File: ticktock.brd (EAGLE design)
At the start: 61 x 67.3 mm, 64 parts, among them IC1 ATMEGA644A, IC2 AD8611RM, IC3 REF200U, J1 AVR_SPI_PRG_6NS, Q1 MOSFET-NCHANNEL2N7002PW, Q2 MOSFET-NCHANNELBSS138, Q3 MOSFET-NCHANNELBSS138, U1 MAX232SOIC16, U2 OSCILLATORSMD, U3 FT232RLSSOP, U4 BMP180

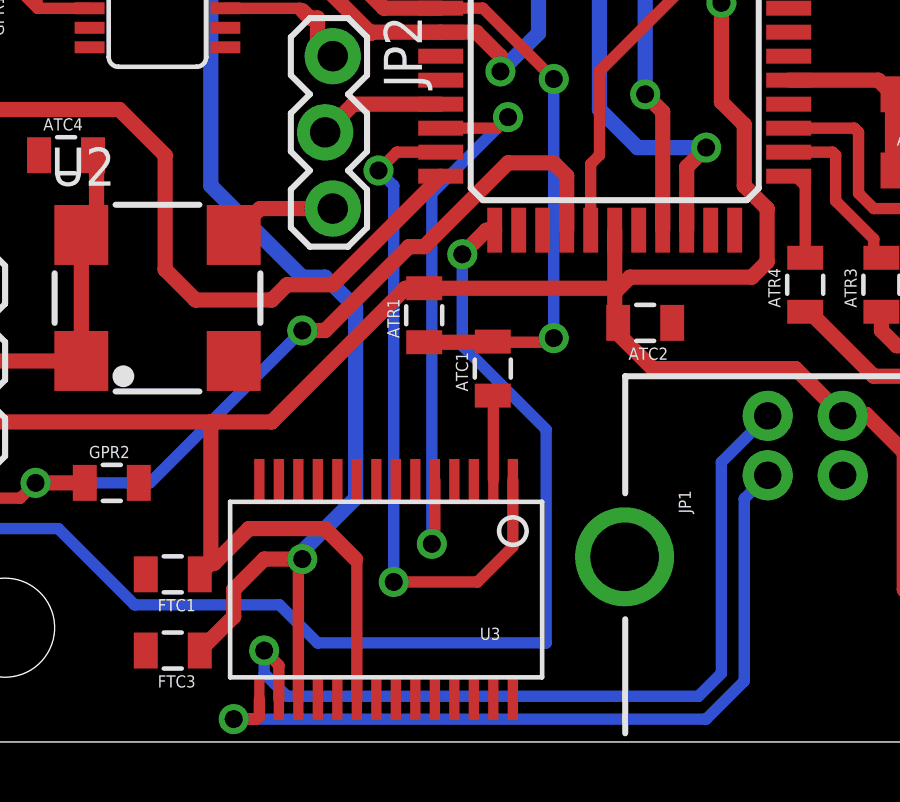
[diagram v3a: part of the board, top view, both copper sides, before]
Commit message: Add power to pin 4 of FTDI chip.
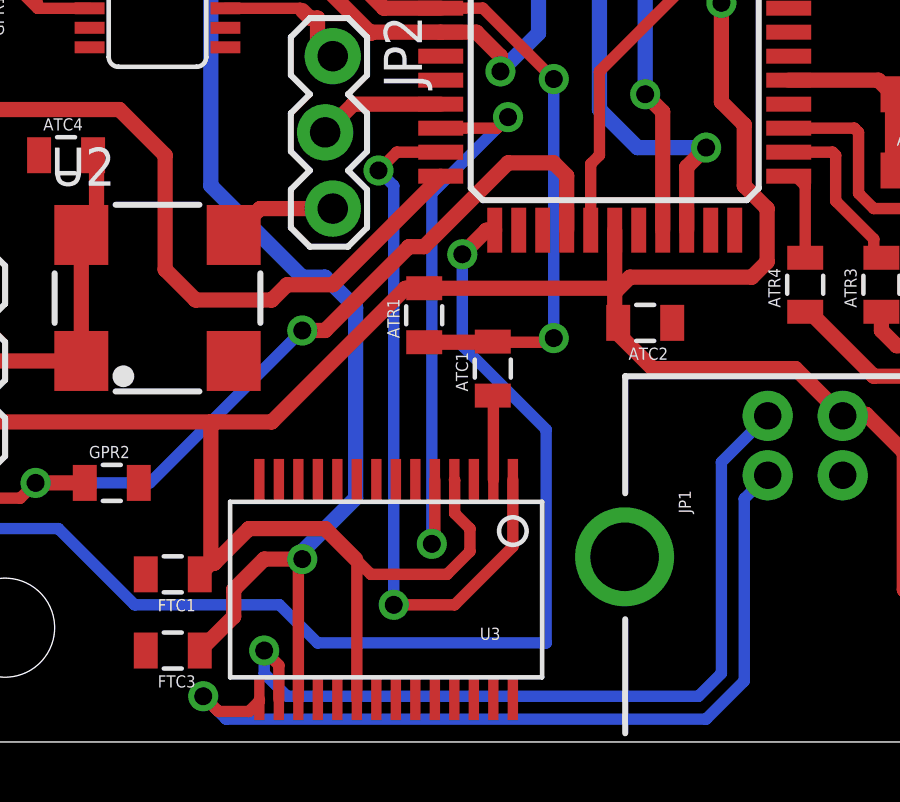
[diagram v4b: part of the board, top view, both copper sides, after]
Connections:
- removed net VCCIO: U3.4
- net 5V: now also U3.4
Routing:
- net 5V: track 295.6 -> 302.5 mm
- net N$12: track 26.2 -> 28.3 mm
- net USB_TX: track 22.9 -> 24.0 mm
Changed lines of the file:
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@@
 </class>
 </classes>
-<designrules name="default">
+<designrules name="default *">
 <description language="de">&lt;b&gt;EAGLE Design Rules&lt;/b&gt;
 &lt;p&gt;
@@
 <param name="mdViaViaSameLayer" value="8mil"/>
 <param name="mnLayersViaInSmd" value="2"/>
-<param name="mdCopperDimension" value="40mil"/>
+<param name="mdCopperDimension" value="20mil"/>
 <param name="mdDrill" value="8mil"/>
 <param name="mdSmdStop" value="0mil"/>
 <param name="msWidth" value="10mil"/>
-<param name="msDrill" value="24mil"/>
+<param name="msDrill" value="23mil"/>
 <param name="msMicroVia" value="9.99mm"/>
 <param name="msBlindViaRatio" value="0.5"/>
@@
 <wire x1="20.597" y1="25.106" x2="21.804" y2="25.106" width="0.381" layer="1"/>
 <wire x1="21.804" y1="25.106" x2="21.844" y2="25.146" width="0.381" layer="1"/>
+<contactref element="U3" pad="4"/>
+<wire x1="29.505" y1="6.055" x2="29.972" y2="5.588" width="0.381" layer="1"/>
+<wire x1="29.972" y1="5.588" x2="32.512" y2="5.588" width="0.381" layer="1"/>
+<wire x1="32.512" y1="5.588" x2="33.274" y2="6.35" width="0.381" layer="1"/>
+<wire x1="33.274" y1="6.35" x2="33.274" y2="7.112" width="0.381" layer="1"/>
+<wire x1="33.274" y1="7.112" x2="32.766" y2="7.62" width="0.381" layer="1"/>
+<wire x1="32.766" y1="7.62" x2="32.766" y2="8.725" width="0.381" layer="1"/>
+<wire x1="32.766" y1="8.725" x2="32.755" y2="8.736" width="0.381" layer="1"/>
 </signal>
 <signal name="N$1">
@@
 <wire x1="18.862" y1="24.456" x2="18.288" y2="25.03" width="0.381" layer="1"/>
 </signal>
-<signal name="VCCIO">
-<contactref element="U3" pad="4"/>
-</signal>
 <signal name="N$11">
 <contactref element="JP1" pad="D-"/>
@@
 <contactref element="U3" pad="15"/>
 <contactref element="JP1" pad="D+"/>
-<wire x1="26.255" y1="1.424" x2="26.255" y2="0.855" width="0.381" layer="1"/>
-<wire x1="26.255" y1="0.855" x2="26.162" y2="0.762" width="0.381" layer="1"/>
-<wire x1="26.162" y1="0.762" x2="25.4" y2="0.762" width="0.381" layer="1"/>
-<via x="25.4" y="0.762" extent="1-16" drill="0.6"/>
-<wire x1="25.4" y1="0.762" x2="41.148" y2="0.762" width="0.381" layer="16"/>
+<wire x1="26.255" y1="1.424" x2="26.255" y2="1.363" width="0.381" layer="1"/>
+<wire x1="26.255" y1="1.363" x2="25.908" y2="1.016" width="0.381" layer="1"/>
+<wire x1="25.908" y1="1.016" x2="24.892" y2="1.016" width="0.381" layer="1"/>
+<wire x1="24.892" y1="1.016" x2="24.384" y2="1.524" width="0.381" layer="1"/>
+<via x="24.384" y="1.524" extent="1-16" drill="0.6"/>
+<wire x1="24.384" y1="1.524" x2="25.146" y2="0.762" width="0.381" layer="16"/>
+<wire x1="25.146" y1="0.762" x2="41.148" y2="0.762" width="0.381" layer="16"/>
 <wire x1="41.148" y1="0.762" x2="42.418" y2="2.032" width="0.381" layer="16"/>
 <wire x1="42.418" y1="2.032" x2="42.418" y2="8.108" width="0.381" layer="16"/>
@@
 <contactref element="IC1" pad="10"/>
 <wire x1="34.705" y1="8.736" x2="34.705" y2="6.511" width="0.381" layer="1"/>
-<wire x1="34.705" y1="6.511" x2="33.528" y2="5.334" width="0.381" layer="1"/>
-<wire x1="33.528" y1="5.334" x2="30.734" y2="5.334" width="0.381" layer="1"/>
-<via x="30.734" y="5.334" extent="1-16" drill="0.6"/>
-<wire x1="30.734" y1="5.334" x2="30.734" y2="18.542" width="0.381" layer="16"/>
+<wire x1="34.705" y1="6.511" x2="32.766" y2="4.572" width="0.381" layer="1"/>
+<via x="30.734" y="4.572" extent="1-16" drill="0.6"/>
+<wire x1="30.734" y1="4.572" x2="30.734" y2="18.542" width="0.381" layer="16"/>
 <wire x1="30.734" y1="18.542" x2="30.226" y2="19.05" width="0.381" layer="16"/>
 <via x="30.226" y="19.05" extent="1-16" drill="0.6"/>
 <wire x1="30.226" y1="19.05" x2="30.836" y2="19.66" width="0.381" layer="1"/>
 <wire x1="30.836" y1="19.66" x2="32.3" y2="19.66" width="0.381" layer="1"/>
+<wire x1="32.766" y1="4.572" x2="30.734" y2="4.572" width="0.381" layer="1"/>
 </signal>
 <signal name="USB_RX">

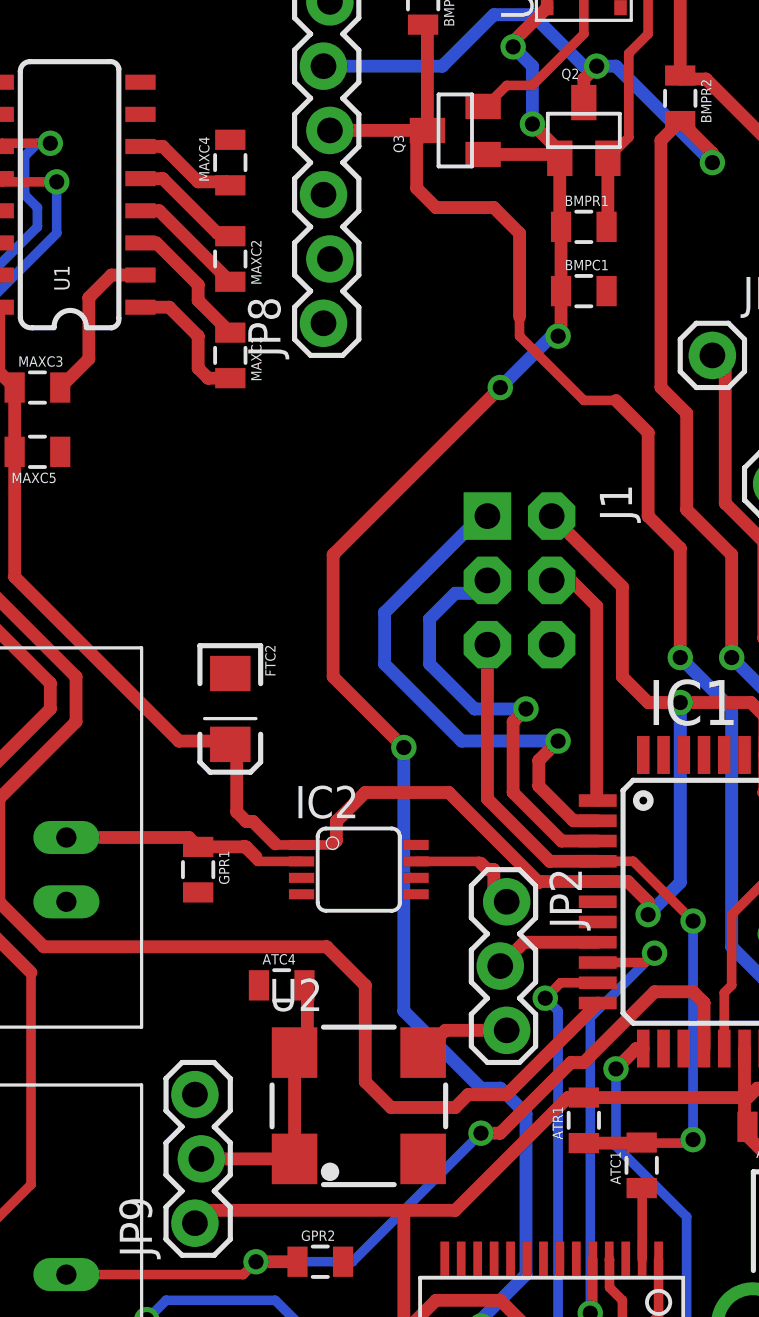
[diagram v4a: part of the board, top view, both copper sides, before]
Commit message: Fix ERC and DRC complaints.  Connect accidentally unconnected nets.
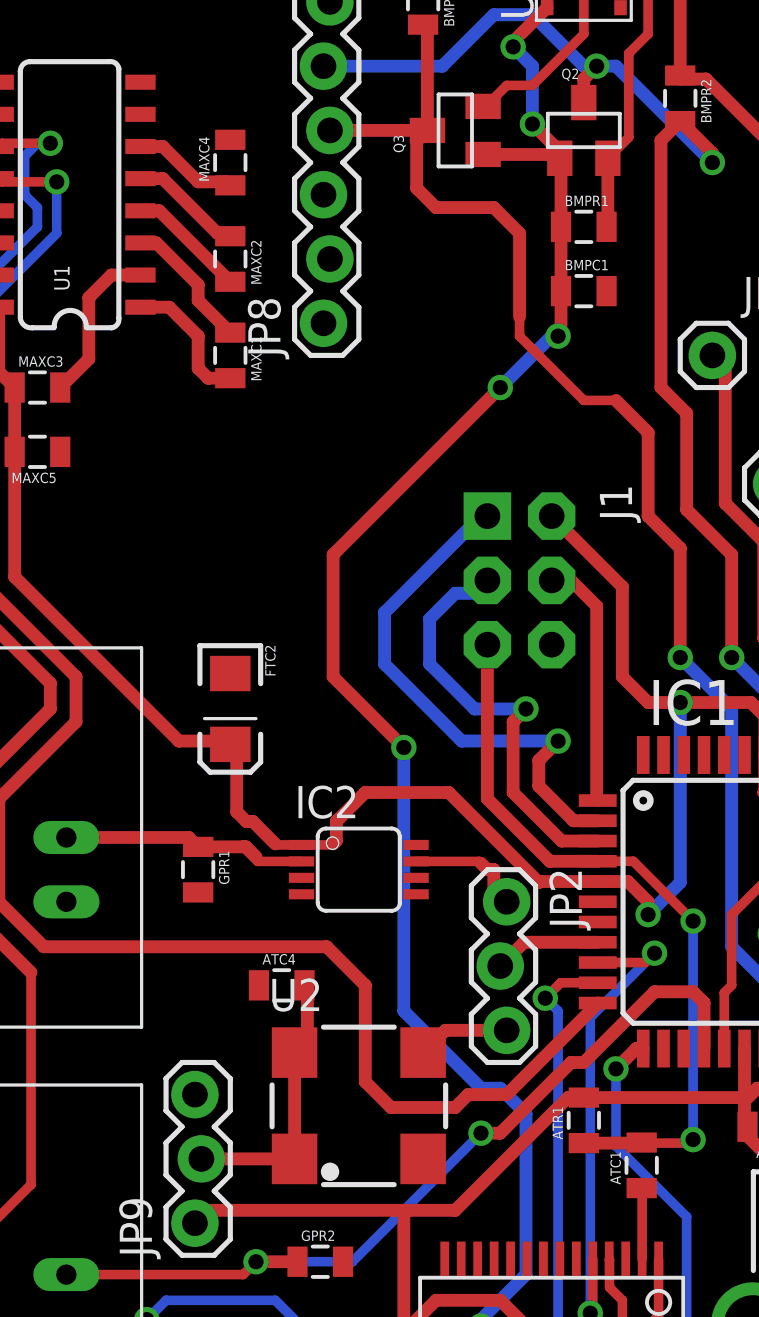
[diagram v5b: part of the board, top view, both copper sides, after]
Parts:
- JP2: value (none) -> 3 Pin
- JP8: value (none) -> 7-Pin
- JP9: value (none) -> 3-Pin
- U$1: value (none) -> OPA381
- X1: value (none) -> RS232
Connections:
- net GND: now also U$1.3, U$1.4
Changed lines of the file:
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@@
 <layer number="35" name="tGlue" color="7" fill="4" visible="no" active="yes"/>
 <layer number="36" name="bGlue" color="7" fill="5" visible="no" active="yes"/>
-<layer number="37" name="tTest" color="7" fill="1" visible="no" active="yes"/>
-<layer number="38" name="bTest" color="7" fill="1" visible="no" active="yes"/>
-<layer number="39" name="tKeepout" color="4" fill="11" visible="yes" active="yes"/>
-<layer number="40" name="bKeepout" color="1" fill="11" visible="yes" active="yes"/>
-<layer number="41" name="tRestrict" color="4" fill="10" visible="yes" active="yes"/>
-<layer number="42" name="bRestrict" color="1" fill="10" visible="yes" active="yes"/>
-<layer number="43" name="vRestrict" color="2" fill="10" visible="yes" active="yes"/>
-<layer number="44" name="Drills" color="7" fill="1" visible="no" active="yes"/>
-<layer number="45" name="Holes" color="7" fill="1" visible="no" active="yes"/>
-<layer number="46" name="Milling" color="3" fill="1" visible="no" active="yes"/>
-<layer number="47" name="Measures" color="7" fill="1" visible="no" active="yes"/>
+<layer number="37" name="tTest" color="7" fill="1" visible="yes" active="yes"/>
+<layer number="38" name="bTest" color="7" fill="1" visible="yes" active="yes"/>
+<layer number="39" name="tKeepout" color="4" fill="11" visible="no" active="yes"/>
+<layer number="40" name="bKeepout" color="1" fill="11" visible="no" active="yes"/>
+<layer number="41" name="tRestrict" color="4" fill="10" visible="no" active="yes"/>
+<layer number="42" name="bRestrict" color="1" fill="10" visible="no" active="yes"/>
+<layer number="43" name="vRestrict" color="2" fill="10" visible="no" active="yes"/>
+<layer number="44" name="Drills" color="7" fill="1" visible="yes" active="yes"/>
+<layer number="45" name="Holes" color="7" fill="1" visible="yes" active="yes"/>
+<layer number="46" name="Milling" color="3" fill="1" visible="yes" active="yes"/>
+<layer number="47" name="Measures" color="7" fill="1" visible="yes" active="yes"/>
 <layer number="48" name="Document" color="7" fill="1" visible="yes" active="yes"/>
 <layer number="49" name="Reference" color="7" fill="1" visible="yes" active="yes"/>
@@
 <element name="MAXC5" library="SparkFun-Capacitors" package="0805" value="1uF" x="10.16" y="40.64" rot="R180"/>
 <element name="MAXC4" library="SparkFun-Capacitors" package="0805" value="1uF" x="17.78" y="52.07" rot="R90"/>
-<element name="X1" library="SparkFun-Connectors" package="DB9" value="" x="3.81" y="50.8" rot="R90"/>
+<element name="X1" library="SparkFun-Connectors" package="DB9" value="RS232" x="3.81" y="50.8" rot="R90"/>
 <element name="GPS_10MHZ_IN" library="SparkFun-Connectors" package="BNC" value="BNCPTH" x="11.303" y="25.4" rot="R90"/>
 <element name="GPS_1PPS_IN" library="SparkFun-Connectors" package="BNC" value="BNCPTH" x="11.303" y="8.128" rot="R90"/>
@@
 <element name="U2" library="SparkFun-FreqCtrl" package="CRYSTAL-SMD-7X5" value="OSCILLATORSMD" x="20.32" y="12.7"/>
 <element name="ATC4" library="SparkFun-Capacitors" package="0805" value="0.01uF" x="19.812" y="19.558"/>
-<element name="JP2" library="SparkFun-Connectors" package="1X03_LOCK" value="" x="28.575" y="22.86" rot="R270"/>
+<element name="JP2" library="SparkFun-Connectors" package="1X03_LOCK" value="3 Pin" x="28.575" y="22.86" rot="R270"/>
 <element name="IC2" library="analog-devices" package="MSOP08" value="AD8611RM" x="22.86" y="24.13" rot="R270">
 <attribute name="OC_NEWARK" value="19M8930" x="22.86" y="24.13" size="1.778" layer="27" rot="R270" display="off"/>
@@
 <element name="CFB" library="SparkFun-Capacitors" package="0805" value="??" x="50.8" y="24.13" rot="R90"/>
 <element name="AMPC1" library="SparkFun-Capacitors" package="0805" value="1uF" x="59.69" y="24.13" rot="R90"/>
-<element name="U$1" library="tickTockLibrary" package="MSOP08" value="" x="56.134" y="20.32" rot="R270"/>
+<element name="U$1" library="tickTockLibrary" package="MSOP08" value="OPA381" x="56.134" y="20.32" rot="R270"/>
 <element name="U4" library="SparkFun-Sensors" package="BMP180" value="BMP180" x="31.75" y="59.69" rot="R90"/>
 <element name="IC3" library="burr-brown" package="SO08" value="REF200U" x="49.53" y="35.56" rot="R270"/>
@@
 <element name="JP6" library="SparkFun-Connectors" package="1X01" value="M01PTH" x="45.72" y="41.91"/>
 <element name="JP7" library="SparkFun-Connectors" package="1X01" value="M01PTH" x="57.15" y="26.67"/>
-<element name="JP8" library="SparkFun-Connectors" package="1X07_LOCK" value="" x="21.59" y="45.72" rot="R90"/>
+<element name="JP8" library="SparkFun-Connectors" package="1X07_LOCK" value="7-Pin" x="21.59" y="45.72" rot="R90"/>
 <element name="STANDOFF1" library="SparkFun-Electromechanical" package="STAND-OFF" value="STAND-OFF" x="57.15" y="63.5"/>
 <element name="STANDOFF2" library="SparkFun-Electromechanical" package="STAND-OFF" value="STAND-OFF" x="10.16" y="63.5"/>
 <element name="STANDOFF3" library="SparkFun-Electromechanical" package="STAND-OFF" value="STAND-OFF" x="56.642" y="15.24"/>
 <element name="STANDOFF4" library="SparkFun-Electromechanical" package="STAND-OFF" value="STAND-OFF" x="17.78" y="3.81"/>
-<element name="JP9" library="SparkFun-Connectors" package="1X03_LOCK" value="" x="16.51" y="10.16" rot="R90"/>
+<element name="JP9" library="SparkFun-Connectors" package="1X03_LOCK" value="3-Pin" x="16.51" y="10.16" rot="R90"/>
 </elements>
 <signals>
@@
 <contactref element="JP8" pad="1"/>
 <contactref element="PKG-CABLE" pad="6"/>
+<contactref element="U$1" pad="3"/>
+<contactref element="U$1" pad="4"/>
 <wire x1="49.96" y1="47.4" x2="49.96" y2="54.2" width="0" layer="19" extent="1-1"/>
 <wire x1="57.6" y1="34.29" x2="49.96" y2="47.4" width="0" layer="19" extent="1-1"/>
@@
 <wire x1="43.9" y1="22.86" x2="46.827" y2="26.782" width="0" layer="19" extent="1-1"/>
 <wire x1="49.16" y1="21.59" x2="43.9" y2="22.86" width="0" layer="19" extent="1-1"/>
+<wire x1="54.021" y1="19.996" x2="49.16" y2="21.59" width="0" layer="19" extent="1-1"/>
+<wire x1="54.021" y1="19.346" x2="54.021" y2="19.996" width="0" layer="19" extent="1-1"/>
 <wire x1="38.9" y1="17.06" x2="43.9" y2="22.86" width="0" layer="19" extent="1-1"/>
 <wire x1="40.016" y1="13.97" x2="38.9" y2="17.06" width="0" layer="19" extent="1-1"/>
@@
 <contactref element="U3" pad="17"/>
 <contactref element="FTC3" pad="1"/>
-<contactref element="BMPR1" pad="1"/>
 <contactref element="BMPR3" pad="1"/>
 <contactref element="U4" pad="2"/>
@@
 <contactref element="Q2" pad="1"/>
 <contactref element="Q3" pad="1"/>
-<wire x1="30.85" y1="49.53" x2="30.734" y2="49.53" width="0.4064" layer="1"/>
-<wire x1="30.734" y1="49.53" x2="30.734" y2="49.784" width="0.4064" layer="1"/>
-<wire x1="30.734" y1="49.784" x2="30.8" y2="49.784" width="0.4064" layer="1"/>
 <wire x1="27.77" y1="52.24" x2="27.77" y2="52.39" width="0.4064" layer="1"/>
-<wire x1="30.85" y1="46.99" x2="30.85" y2="49.53" width="0.508" layer="1"/>
-<wire x1="30.8" y1="49.784" x2="30.8" y2="52.24" width="0.508" layer="1"/>
 <wire x1="30.8" y1="52.24" x2="30.65" y2="52.39" width="0.508" layer="1"/>
 <wire x1="30.65" y1="52.39" x2="27.77" y2="52.39" width="0.508" layer="1"/>
@@
 <wire x1="27.555" y1="1.424" x2="27.555" y2="5.965" width="0.381" layer="1"/>
 <wire x1="27.555" y1="5.965" x2="27.686" y2="6.096" width="0.381" layer="1"/>
+<contactref element="BMPR1" pad="1"/>
+<wire x1="30.85" y1="49.53" x2="30.85" y2="52.19" width="0.508" layer="1"/>
+<wire x1="30.85" y1="52.19" x2="30.8" y2="52.24" width="0.508" layer="1"/>
+<wire x1="30.85" y1="49.53" x2="30.85" y2="46.99" width="0.508" layer="1"/>
 </signal>
 <signal name="USB_DTR">
@@
 <contactref element="ATC4" pad="2"/>
 <contactref element="JP9" pad="2"/>
-<wire x1="16.51" y1="12.7" x2="20.32" y2="12.7" width="0.508" layer="1"/>
 <wire x1="20.32" y1="12.7" x2="20.32" y2="16.9" width="0.508" layer="1"/>
 <wire x1="20.712" y1="19.558" x2="20.828" y2="19.442" width="0.508" layer="1"/>
@@
 <wire x1="20.828" y1="17.526" x2="20.32" y2="17.018" width="0.508" layer="1"/>
 <wire x1="20.32" y1="17.018" x2="20.32" y2="16.9" width="0.508" layer="1"/>
-<wire x1="16.51" y1="12.7" x2="16.637" y2="12.7" width="0" layer="19" extent="1-1"/>
+<wire x1="16.637" y1="12.7" x2="20.32" y2="12.7" width="0.508" layer="1"/>
 </signal>
 <signal name="N$16">
